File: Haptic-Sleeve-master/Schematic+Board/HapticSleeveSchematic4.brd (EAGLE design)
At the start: 60.6 x 38.1 mm, 11 parts, among them M1 F-1X02-SIP-100-40, M2 F-1X02-SIP-100-40, M3 F-1X02-SIP-100-40, M4 F-1X02-SIP-100-40

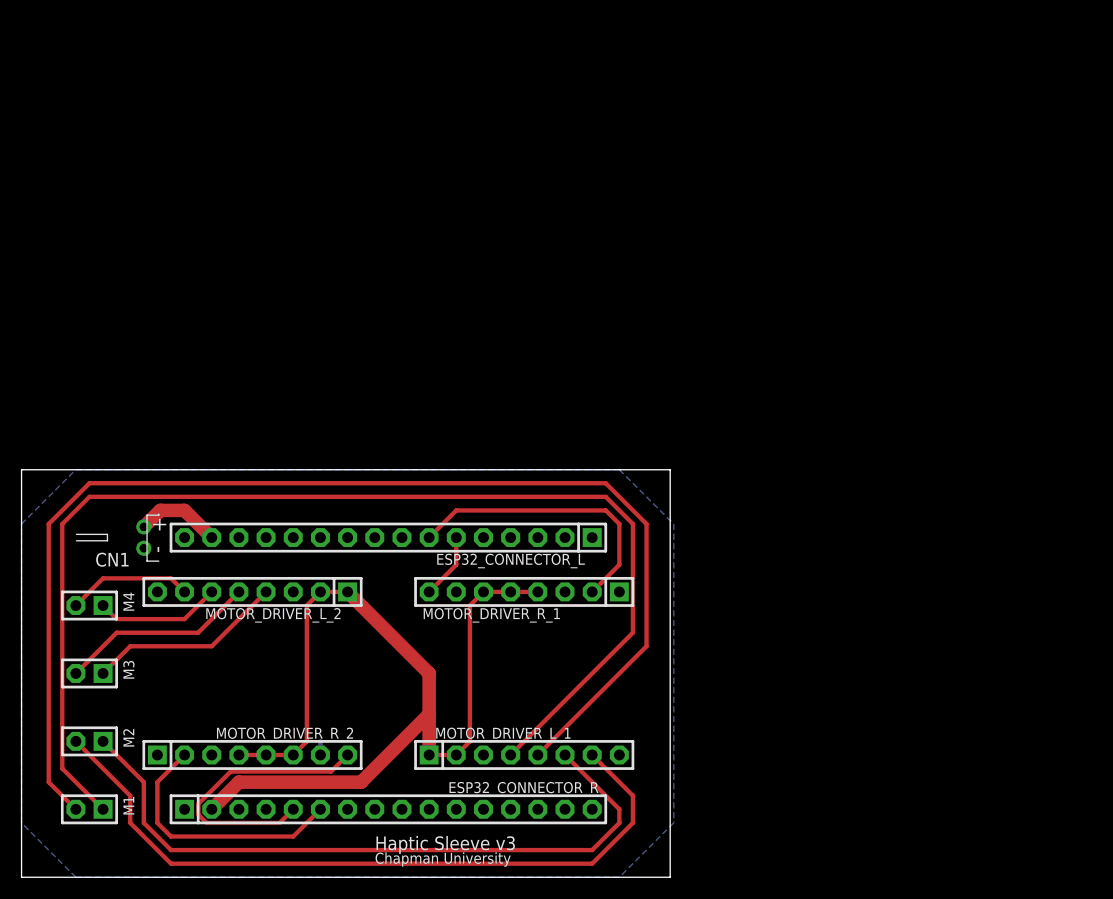
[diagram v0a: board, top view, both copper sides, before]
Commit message: HapticSleeveSchematic3.brd has 4 motors on one side of board with more routing. HapticSleeveSchematic3 - Copy.brd has 2 motors on each side of the board with less routing
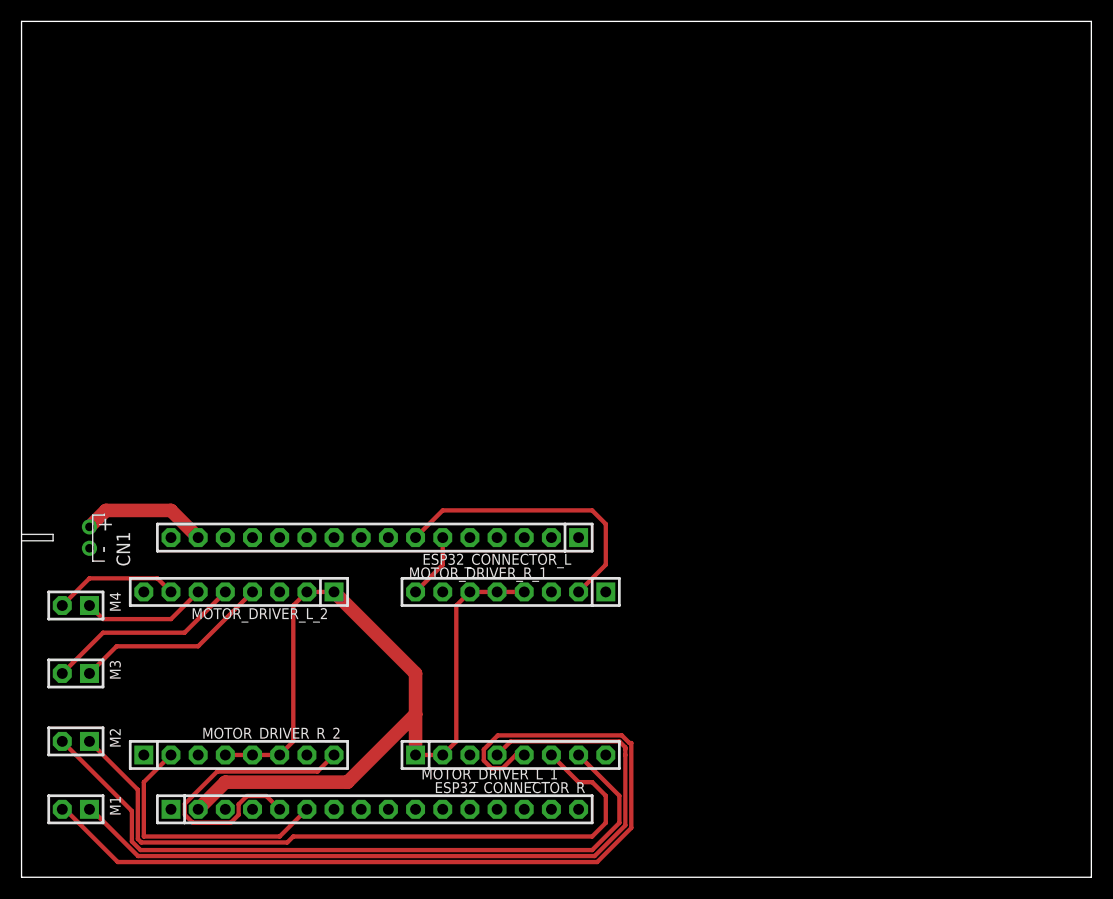
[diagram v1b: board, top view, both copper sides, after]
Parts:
- moved CN1 5.08 mm to (6.35, 31.8)
- moved MOTOR_DRIVER_L_1 1.27 mm to (45.7, 11.4)
- moved MOTOR_DRIVER_R_1 1.27 mm to (45.7, 26.7)
- moved M1 1.27 mm to (5.08, 6.35)
- moved M2 1.27 mm to (5.08, 12.7)
- moved M3 1.27 mm to (5.08, 19.1)
- moved M4 1.27 mm to (5.08, 25.4)
- moved MOTOR_DRIVER_L_2 1.27 mm to (20.3, 26.7)
- moved MOTOR_DRIVER_R_2 1.27 mm to (20.3, 11.4)
- moved ESP32_CONNECTOR_L 1.27 mm to (33.0, 31.8)
- moved ESP32_CONNECTOR_R 1.27 mm to (33.0, 6.35)
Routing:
- net M1+: track 110.2 -> 73.1 mm
- net M1-: track 112.8 -> 84.7 mm
- net VCC: track 8.04 -> 11.8 mm
- net MOTOR3: track 26.6 -> 28.2 mm
- net GND: track 1.27 -> 0.00 mm
- net M2-: track 67.8 -> 66.9 mm
- net MOTOR4: track 24.2 -> 25.0 mm
- net M2+: track 64.2 -> 64.8 mm
- removed copper zone on layer 16, net GND
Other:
- board size 60.6 x 38.1 mm -> 100 x 80 mm
- board text removed: "Chapman University"
- board text removed: "Haptic Sleeve v3"
